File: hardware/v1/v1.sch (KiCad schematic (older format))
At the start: 0 parts

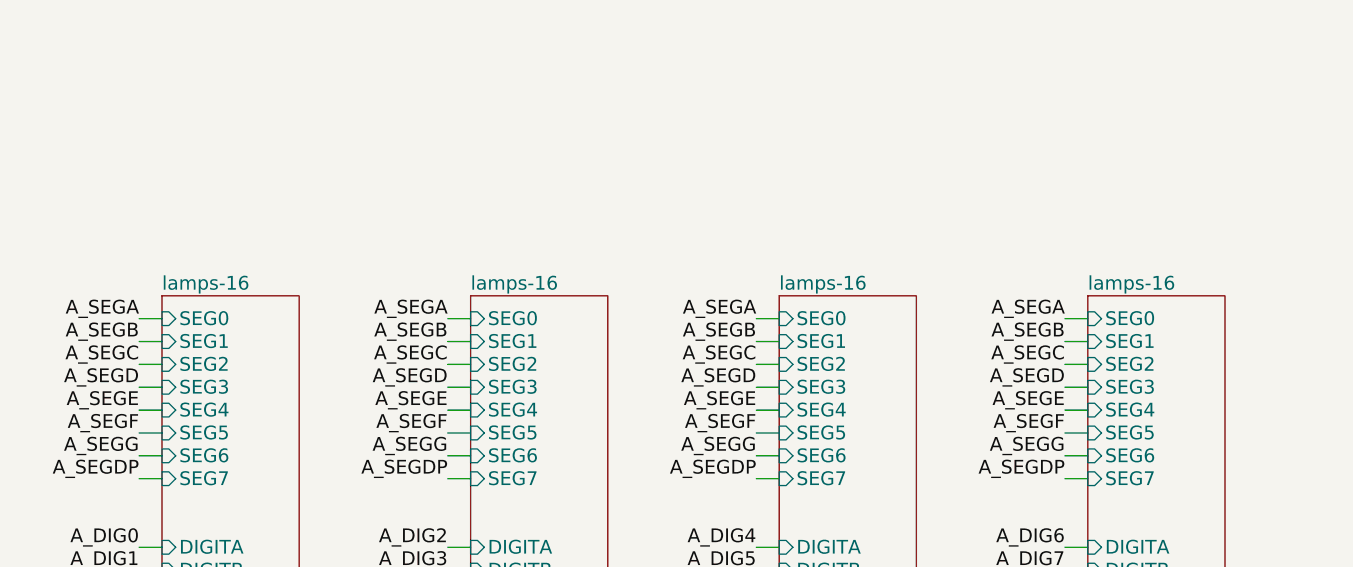
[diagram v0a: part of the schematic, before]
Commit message: Some autorouting on 16led row
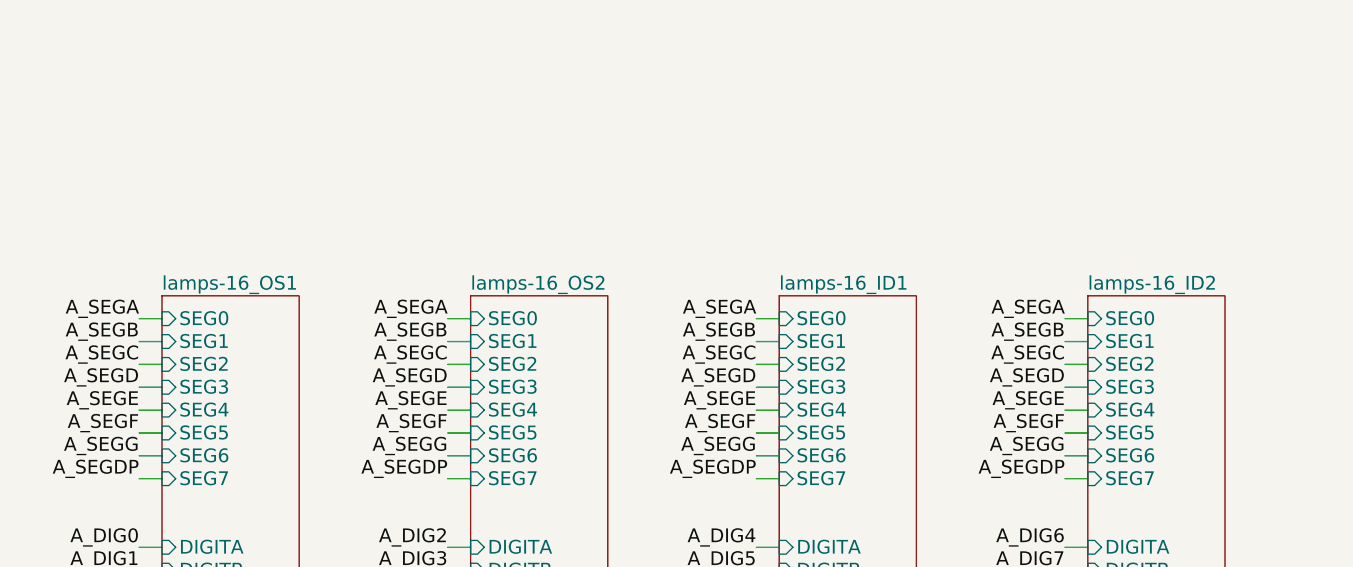
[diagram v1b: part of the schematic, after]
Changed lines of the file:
@@
 S 6200 650  600  1300
 U 57A49D32
-F0 "lamps-16" 60
+F0 "lamps-16_OS1" 60
 F1 "lamps-16.sch" 60
 F2 "SEG0" I L 6200 750 60
@@
 S 7550 650  600  1300
 U 57A54838
-F0 "lamps-16" 60
+F0 "lamps-16_OS2" 60
 F1 "lamps-16.sch" 60
 F2 "SEG0" I L 7550 750 60
@@
 S 8900 650  600  1300
 U 57A56102
-F0 "lamps-16" 60
+F0 "lamps-16_ID1" 60
 F1 "lamps-16.sch" 60
 F2 "SEG0" I L 8900 750 60
@@
 S 10250 650  600  1300
 U 57A56122
-F0 "lamps-16" 60
+F0 "lamps-16_ID2" 60
 F1 "lamps-16.sch" 60
 F2 "SEG0" I L 10250 750 60
